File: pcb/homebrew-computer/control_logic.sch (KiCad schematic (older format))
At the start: 14 parts

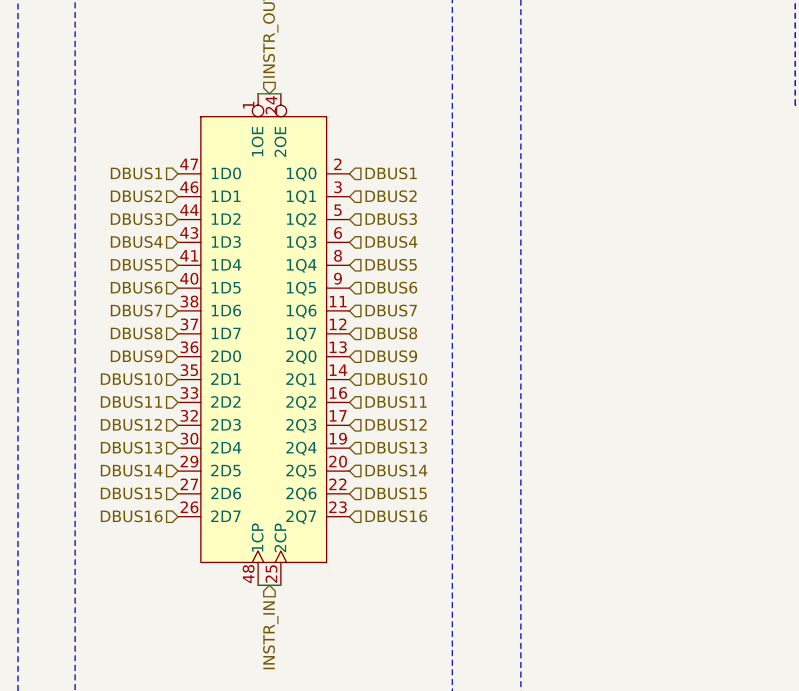
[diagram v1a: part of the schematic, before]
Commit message: Add the memory interface logic
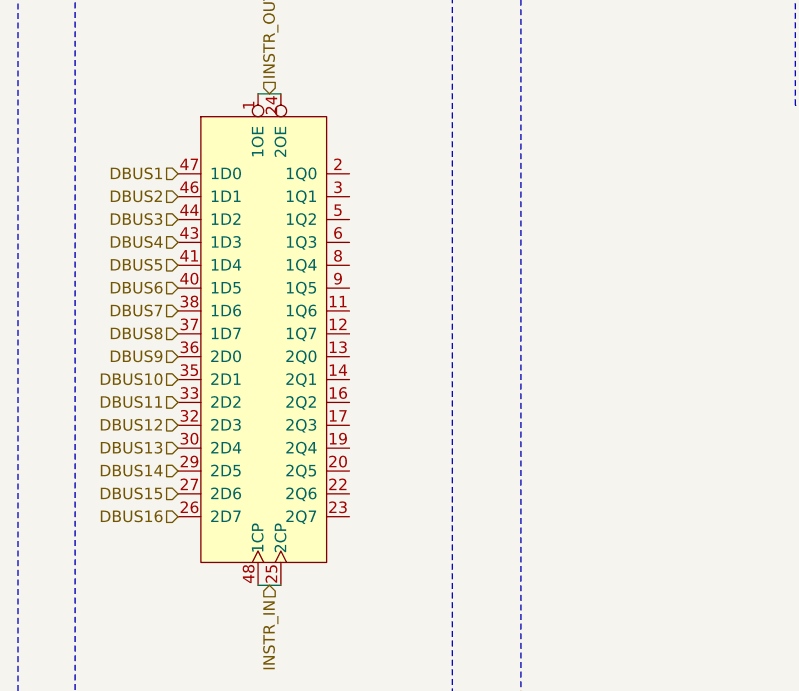
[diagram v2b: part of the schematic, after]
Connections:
- net DBUS1: no longer U?.2 (1Q0)
- net DBUS10: no longer U?.14 (2Q1)
- net DBUS11: no longer U?.16 (2Q2)
- net DBUS12: no longer U?.17 (2Q3)
- net DBUS13: no longer U?.19 (2Q4)
- net DBUS14: no longer U?.20 (2Q5)
- net DBUS15: no longer U?.22 (2Q6)
- net DBUS16: no longer U?.23 (2Q7)
- net DBUS2: no longer U?.3 (1Q1)
- net DBUS3: no longer U?.5 (1Q2)
- net DBUS4: no longer U?.6 (1Q3)
- net DBUS5: no longer U?.8 (1Q4)
- net DBUS6: no longer U?.9 (1Q5)
- net DBUS7: no longer U?.11 (1Q6)
- net DBUS8: no longer U?.12 (1Q7)
- net DBUS9: no longer U?.13 (2Q0)
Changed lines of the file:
@@
 Text Notes 1200 5100 0    50   ~ 0
 Power
-Text HLabel 2450 2400 2    50   Input ~ 0
-DBUS1
-Text HLabel 2450 2500 2    50   Input ~ 0
-DBUS2
-Text HLabel 2450 2600 2    50   Input ~ 0
-DBUS3
-Text HLabel 2450 2700 2    50   Input ~ 0
-DBUS4
-Text HLabel 2450 2800 2    50   Input ~ 0
-DBUS5
-Text HLabel 2450 2900 2    50   Input ~ 0
-DBUS6
-Text HLabel 2450 3000 2    50   Input ~ 0
-DBUS7
-Text HLabel 2450 3100 2    50   Input ~ 0
-DBUS8
-Text HLabel 2450 3200 2    50   Input ~ 0
-DBUS9
-Text HLabel 2450 3300 2    50   Input ~ 0
-DBUS10
-Text HLabel 2450 3400 2    50   Input ~ 0
-DBUS11
-Text HLabel 2450 3500 2    50   Input ~ 0
-DBUS12
-Text HLabel 2450 3600 2    50   Input ~ 0
-DBUS13
-Text HLabel 2450 3700 2    50   Input ~ 0
-DBUS14
-Text HLabel 2450 3800 2    50   Input ~ 0
-DBUS15
-Text HLabel 2450 3900 2    50   Input ~ 0
-DBUS16
 Text HLabel 1700 2400 0    50   Input ~ 0
 DBUS1

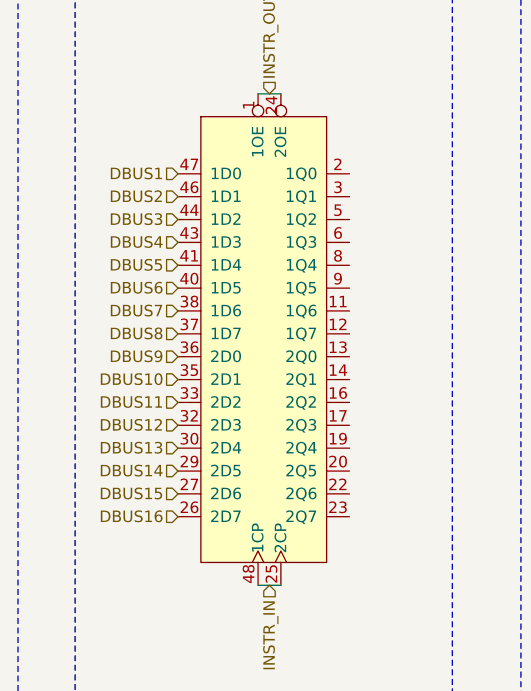
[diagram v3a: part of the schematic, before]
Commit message: Remove the address bus as it would require too big of a connector
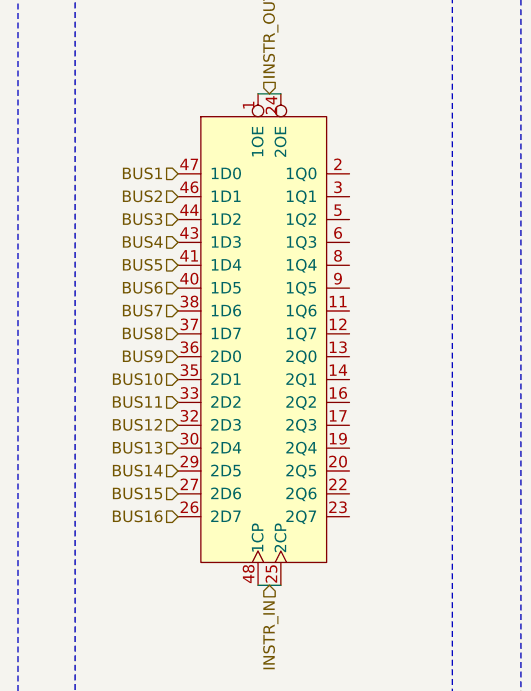
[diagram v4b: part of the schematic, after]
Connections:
- net DBUS1 renamed BUS1
- net DBUS10 renamed BUS10
- net DBUS11 renamed BUS11
- net DBUS12 renamed BUS12
- net DBUS13 renamed BUS13
- net DBUS14 renamed BUS14
- net DBUS15 renamed BUS15
- net DBUS16 renamed BUS16
- net DBUS2 renamed BUS2
- net DBUS3 renamed BUS3
- net DBUS4 renamed BUS4
- net DBUS5 renamed BUS5
- net DBUS6 renamed BUS6
- net DBUS7 renamed BUS7
- net DBUS8 renamed BUS8
- net DBUS9 renamed BUS9
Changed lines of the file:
@@
 $Descr User 8661 8268
 encoding utf-8
-Sheet 3 8
+Sheet 2 7
 Title ""
 Date ""
@@
 Text Notes 1200 5100 0    50   ~ 0
 Power
-Text HLabel 1700 2400 0    50   Input ~ 0
-DBUS1
-Text HLabel 1700 2500 0    50   Input ~ 0
-DBUS2
-Text HLabel 1700 2600 0    50   Input ~ 0
-DBUS3
-Text HLabel 1700 2700 0    50   Input ~ 0
-DBUS4
-Text HLabel 1700 2800 0    50   Input ~ 0
-DBUS5
-Text HLabel 1700 2900 0    50   Input ~ 0
-DBUS6
-Text HLabel 1700 3000 0    50   Input ~ 0
-DBUS7
-Text HLabel 1700 3100 0    50   Input ~ 0
-DBUS8
-Text HLabel 1700 3200 0    50   Input ~ 0
-DBUS9
-Text HLabel 1700 3300 0    50   Input ~ 0
-DBUS10
-Text HLabel 1700 3400 0    50   Input ~ 0
-DBUS11
-Text HLabel 1700 3500 0    50   Input ~ 0
-DBUS12
-Text HLabel 1700 3600 0    50   Input ~ 0
-DBUS13
-Text HLabel 1700 3700 0    50   Input ~ 0
-DBUS14
-Text HLabel 1700 3800 0    50   Input ~ 0
-DBUS15
-Text HLabel 1700 3900 0    50   Input ~ 0
-DBUS16
 Wire Notes Line
 	1250 1250 2900 1250
@@
 Text HLabel 2100 4200 3    50   Input ~ 0
 INSTR_IN
+Text HLabel 1700 2400 0    50   Input ~ 0
+BUS1
+Text HLabel 1700 2500 0    50   Input ~ 0
+BUS2
+Text HLabel 1700 2600 0    50   Input ~ 0
+BUS3
+Text HLabel 1700 2700 0    50   Input ~ 0
+BUS4
+Text HLabel 1700 2800 0    50   Input ~ 0
+BUS5
+Text HLabel 1700 2900 0    50   Input ~ 0
+BUS6
+Text HLabel 1700 3000 0    50   Input ~ 0
+BUS7
+Text HLabel 1700 3100 0    50   Input ~ 0
+BUS8
+Text HLabel 1700 3200 0    50   Input ~ 0
+BUS9
+Text HLabel 1700 3300 0    50   Input ~ 0
+BUS10
+Text HLabel 1700 3400 0    50   Input ~ 0
+BUS11
+Text HLabel 1700 3500 0    50   Input ~ 0
+BUS12
+Text HLabel 1700 3600 0    50   Input ~ 0
+BUS13
+Text HLabel 1700 3700 0    50   Input ~ 0
+BUS14
+Text HLabel 1700 3800 0    50   Input ~ 0
+BUS15
+Text HLabel 1700 3900 0    50   Input ~ 0
+BUS16
 $EndSCHEMATC

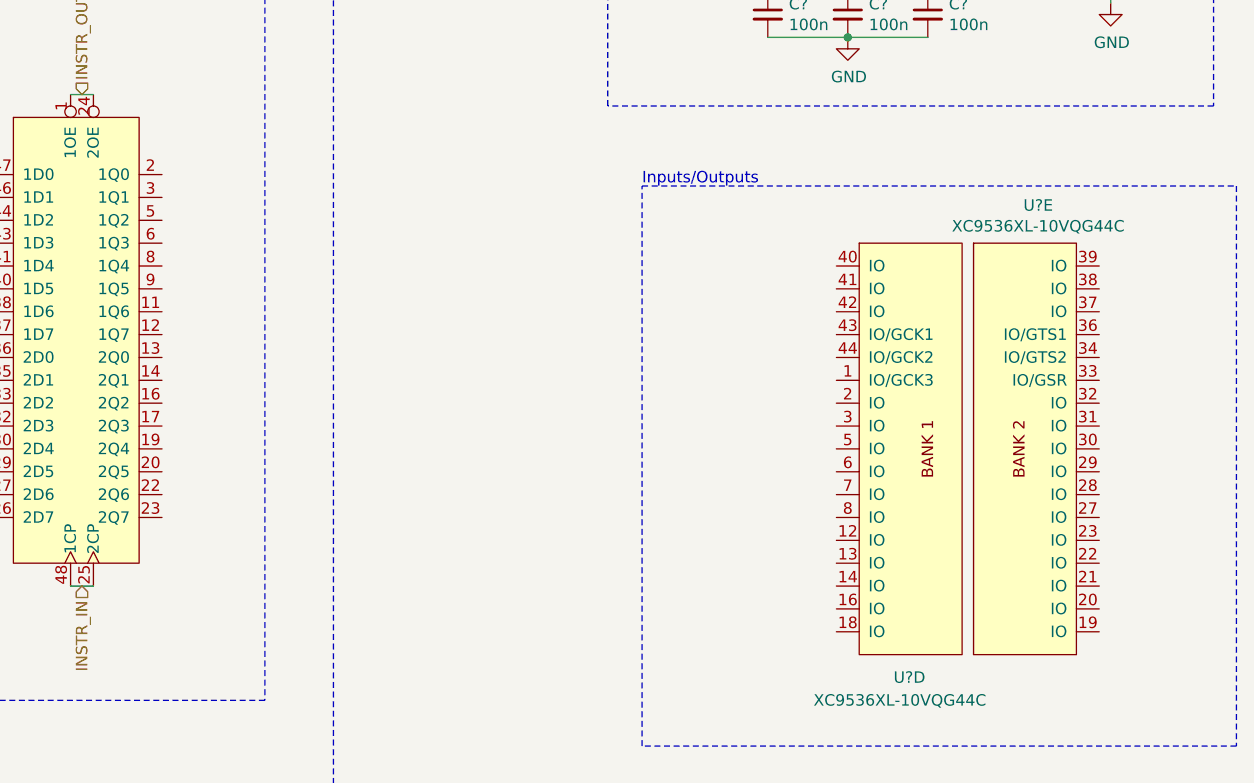
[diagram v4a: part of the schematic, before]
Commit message: Remove unnecessary address bus and unified the IO interface
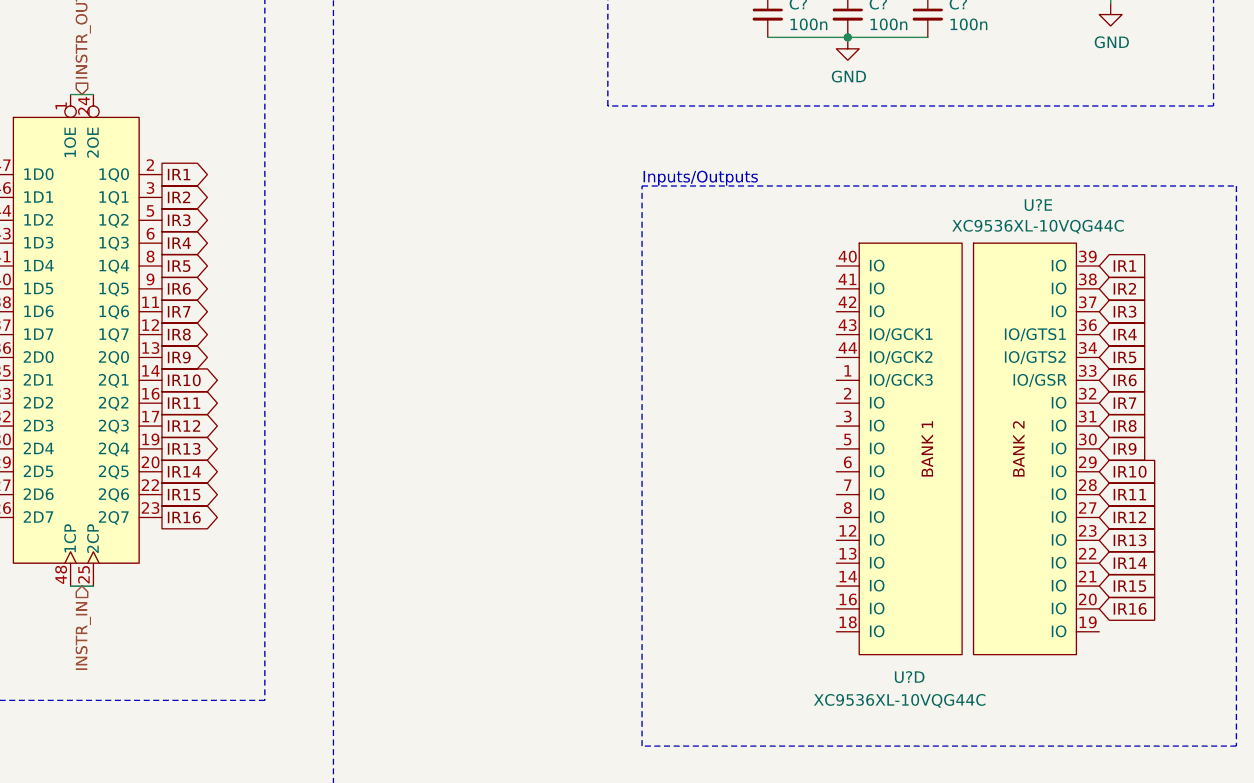
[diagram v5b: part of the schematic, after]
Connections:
- net IR16: now reaches U?.20 (IO)
- net IR16: now also U?.23 (2Q7)
- net IR15: now reaches U?.21 (IO)
- net IR15: now also U?.22 (2Q6)
- net IR14: now reaches U?.22 (IO)
- net IR14: now also U?.20 (2Q5)
- net IR13: now reaches U?.23 (IO)
- net IR13: now also U?.19 (2Q4)
- net IR12: now reaches U?.27 (IO)
- net IR12: now also U?.17 (2Q3)
- net IR11: now reaches U?.28 (IO)
- net IR11: now also U?.16 (2Q2)
- net IR10: now reaches U?.29 (IO)
- net IR10: now also U?.14 (2Q1)
- net IR9: now reaches U?.30 (IO)
- net IR9: now also U?.13 (2Q0)
- net IR8: now reaches U?.31 (IO)
- net IR8: now also U?.12 (1Q7)
- net IR7: now reaches U?.32 (IO)
- net IR7: now also U?.11 (1Q6)
- net IR6: now reaches U?.33 (IO/GSR)
- net IR6: now also U?.9 (1Q5)
- net IR5: now reaches U?.34 (IO/GTS2)
- net IR5: now also U?.8 (1Q4)
- net IR4: now reaches U?.36 (IO/GTS1)
- net IR4: now also U?.6 (1Q3)
- net IR3: now reaches U?.37 (IO)
- net IR3: now also U?.5 (1Q2)
- net IR2: now reaches U?.38 (IO)
- net IR2: now also U?.3 (1Q1)
- net IR1: now reaches U?.39 (IO)
- net IR1: now also U?.2 (1Q0)
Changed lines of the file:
@@
 $Descr User 8661 8268
 encoding utf-8
-Sheet 2 7
+Sheet 5 7
 Title ""
 Date ""
@@
 Text HLabel 1700 3900 0    50   Input ~ 0
 BUS16
+Text GLabel 2450 2400 2    50   Output ~ 0
+IR1
+Text GLabel 2450 2500 2    50   Output ~ 0
+IR2
+Text GLabel 2450 2600 2    50   Output ~ 0
+IR3
+Text GLabel 2450 2700 2    50   Output ~ 0
+IR4
+Text GLabel 2450 2800 2    50   Output ~ 0
+IR5
+Text GLabel 2450 2900 2    50   Output ~ 0
+IR6
+Text GLabel 2450 3000 2    50   Output ~ 0
+IR7
+Text GLabel 2450 3100 2    50   Output ~ 0
+IR8
+Text GLabel 2450 3200 2    50   Output ~ 0
+IR9
+Text GLabel 2450 3300 2    50   Output ~ 0
+IR10
+Text GLabel 2450 3400 2    50   Output ~ 0
+IR11
+Text GLabel 2450 3500 2    50   Output ~ 0
+IR12
+Text GLabel 2450 3600 2    50   Output ~ 0
+IR13
+Text GLabel 2450 3700 2    50   Output ~ 0
+IR14
+Text GLabel 2450 3800 2    50   Output ~ 0
+IR15
+Text GLabel 2450 3900 2    50   Output ~ 0
+IR16
+Text GLabel 6550 2800 2    50   Input ~ 0
+IR1
+Text GLabel 6550 2900 2    50   Input ~ 0
+IR2
+Text GLabel 6550 3000 2    50   Input ~ 0
+IR3
+Text GLabel 6550 3100 2    50   Input ~ 0
+IR4
+Text GLabel 6550 3200 2    50   Input ~ 0
+IR5
+Text GLabel 6550 3300 2    50   Input ~ 0
+IR6
+Text GLabel 6550 3400 2    50   Input ~ 0
+IR7
+Text GLabel 6550 3500 2    50   Input ~ 0
+IR8
+Text GLabel 6550 3600 2    50   Input ~ 0
+IR9
+Text GLabel 6550 3700 2    50   Input ~ 0
+IR10
+Text GLabel 6550 3800 2    50   Input ~ 0
+IR11
+Text GLabel 6550 3900 2    50   Input ~ 0
+IR12
+Text GLabel 6550 4000 2    50   Input ~ 0
+IR13
+Text GLabel 6550 4100 2    50   Input ~ 0
+IR14
+Text GLabel 6550 4200 2    50   Input ~ 0
+IR15
+Text GLabel 6550 4300 2    50   Input ~ 0
+IR16
 $EndSCHEMATC

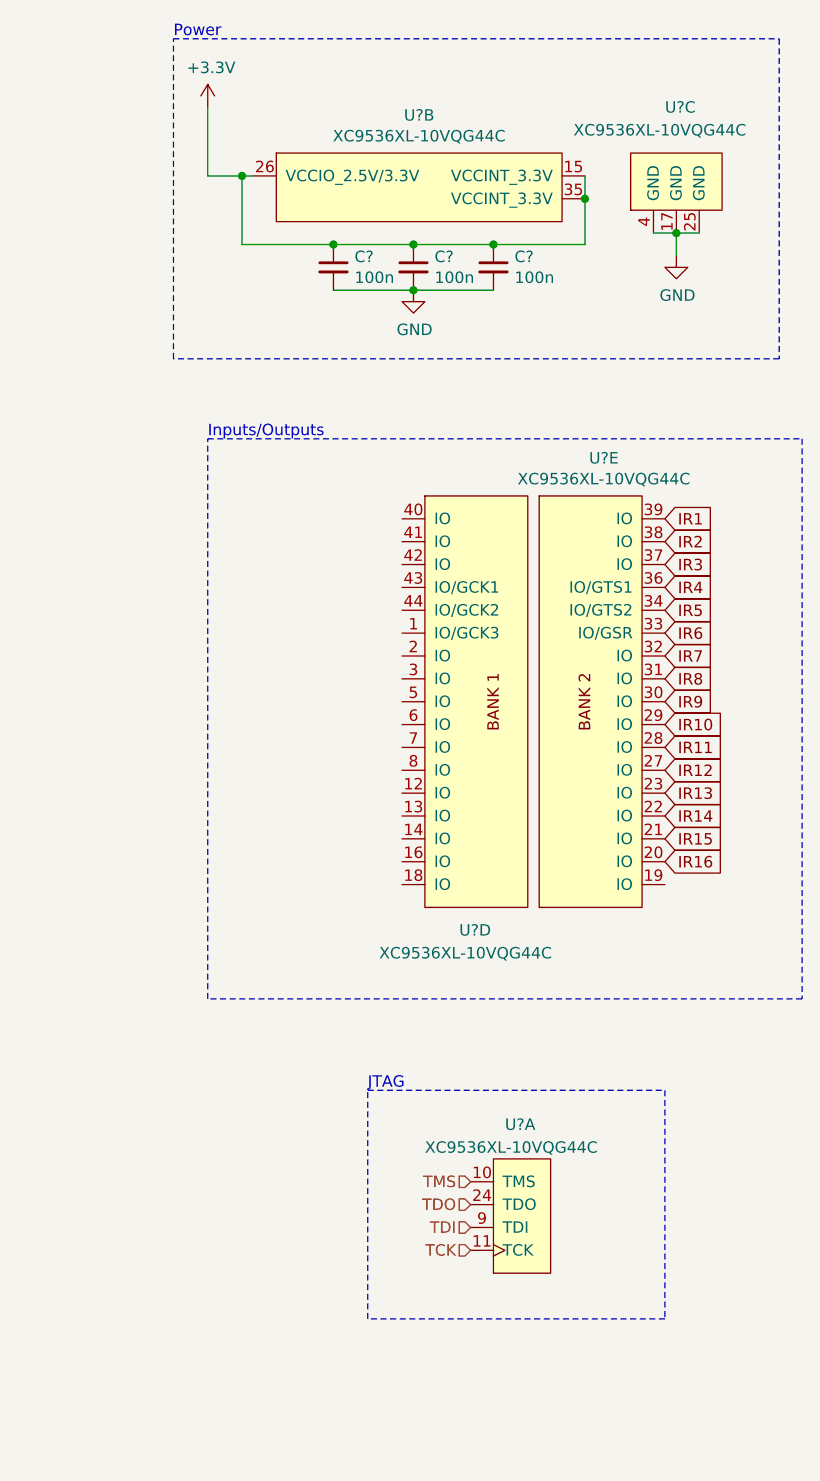
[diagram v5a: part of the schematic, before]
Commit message: Add program counter
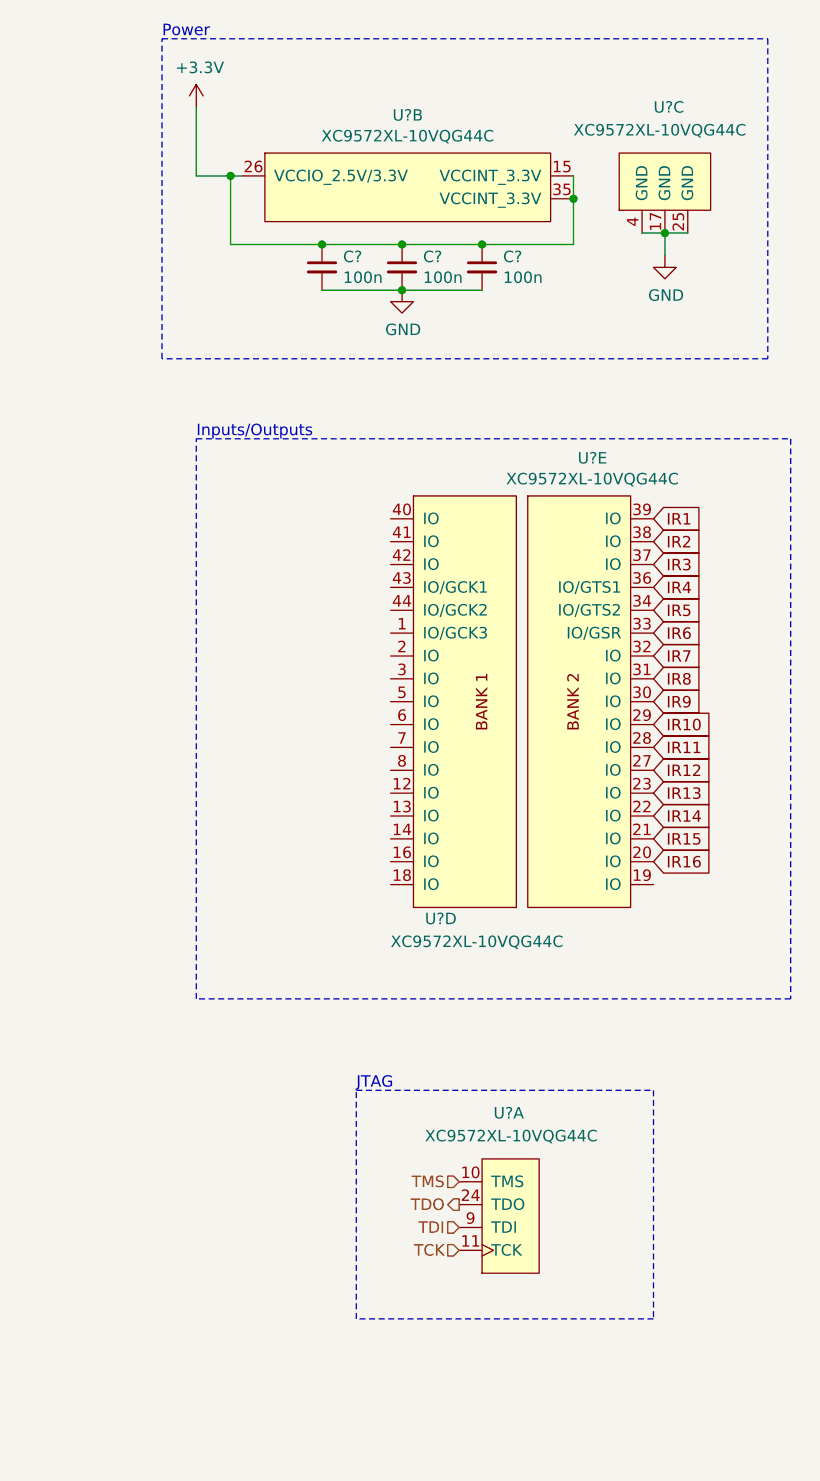
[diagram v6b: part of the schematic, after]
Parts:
- removed U? (x5): XC9536XL-10VQG44C, symbol XC9500XL:XC9536XL-10VQG44C
- added U? (x5): XC9572XL-10VQG44C, symbol XC9500XL:XC9572XL-10VQG44C
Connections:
- net +3V3: now also U?.15 (VCCINT_3.3V), U?.26 (VCCIO_2.5V/3.3V), U?.35 (VCCINT_3.3V)
- net GND: now also U?.17 (GND), U?.25 (GND), U?.4 (GND)
- net IR1: now also U?.39 (IO)
- net IR10: now also U?.29 (IO)
- net IR11: now also U?.28 (IO)
- net IR12: now also U?.27 (IO)
- net IR13: now also U?.23 (IO)
- net IR14: now also U?.22 (IO)
- net IR15: now also U?.21 (IO)
- net IR16: now also U?.20 (IO)
- net IR2: now also U?.38 (IO)
- net IR3: now also U?.37 (IO)
- net IR4: now also U?.36 (IO/GTS1)
- net IR5: now also U?.34 (IO/GTS2)
- net IR6: now also U?.33 (IO/GSR)
- net IR7: now also U?.32 (IO)
- net IR8: now also U?.31 (IO)
- net IR9: now also U?.30 (IO)
- net TCK: now also U?.11 (TCK)
- net TDI: now also U?.9 (TDI)
- net TDO: now also U?.24 (TDO)
- net TMS: now also U?.10 (TMS)
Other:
- moved on the sheet: C?
